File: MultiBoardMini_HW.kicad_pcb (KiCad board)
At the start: 2 copper layers, 63 x 63 mm, 52 parts, among them J1 PB0, J2 PA10, J3 Conn_01x02_Male, J4 PA10, J6 Conn_01x04, SW1 PF1, SW2 RESET, SW3 SW_Push_DPDT, SW5 SW_Push_DPDT, T3 PTS_1.5_2, U1 M78AR5-1, U2 NUCLEO-F303K8, U3 ESP32-C3-WROOM-02-N4, U4 TB67H303HG, U5 TB67H303HG, U6 MCP2562-E_SN

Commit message: 配線一応できた
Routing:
- net +5V: track 3.38 -> 145.1 mm
- net Net-(ENC/IO_2-Pin_4): track 0.00 -> 79.1 mm, vias 0 -> 5
- net Net-(ENC/IO_2-Pin_3): track 0.00 -> 66.0 mm, vias 0 -> 2
- net Net-(U2A-PA8): track 0.00 -> 64.9 mm, vias 0 -> 3
- net +3V3: track 84.7 -> 142.9 mm, vias 0 -> 2
- net Net-(D1-A): track 0.00 -> 56.5 mm, vias 0 -> 6
- net Net-(J6-Pin_1): track 0.00 -> 50.8 mm, vias 0 -> 3
- net Net-(U2B-PA5): track 0.00 -> 43.3 mm
- net Net-(U2A-NRST_1): track 0.00 -> 43.0 mm, vias 0 -> 1
- net Net-(U2B-PB3): track 0.00 -> 40.9 mm, vias 0 -> 1
- net Net-(U2A-PB0): track 0.00 -> 39.5 mm, vias 0 -> 2
- net Net-(U2A-PB4): track 0.00 -> 37.8 mm, vias 0 -> 1
- net Net-(J6-Pin_2): track 0.00 -> 36.0 mm, vias 0 -> 1
- net Net-(U2A-PB1): track 0.00 -> 35.9 mm, vias 0 -> 1
- net Net-(U4-VREG): track 0.00 -> 34.1 mm, vias 0 -> 1
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
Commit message: 配線一応完了 DRC確認済み
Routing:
- net GND: vias 114 -> 122
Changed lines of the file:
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@@
   (via (at 9 -8.5) (size 0.8) (drill 0.4) (layers "F.Cu" "B.Cu") (free) (net 2))
   (via (at -11.95 4.95) (size 0.5) (drill 0.3) (layers "F.Cu" "B.Cu") (free) (net 2))
+  (via (at -15 30) (size 0.8) (drill 0.4) (layers "F.Cu" "B.Cu") (free) (net 2))
+  (via (at 12.5 30) (size 0.8) (drill 0.4) (layers "F.Cu" "B.Cu") (free) (net 2))
+  (via (at 10.5 30) (size 0.8) (drill 0.4) (layers "F.Cu" "B.Cu") (free) (net 2))
+  (via (at -13 30) (size 0.8) (drill 0.4) (layers "F.Cu" "B.Cu") (free) (net 2))
   (via (at -13.75 -11.75) (size 0.5) (drill 0.3) (layers "F.Cu" "B.Cu") (free) (net 2))
   (via (at 16.75 12.25) (size 0.8) (drill 0.4) (layers "F.Cu" "B.Cu") (free) (net 2))
@@
   (via (at -12.4 9.8) (size 0.5) (drill 0.3) (layers "F.Cu" "B.Cu") (free) (net 2))
   (via (at 10 4) (size 0.8) (drill 0.4) (layers "F.Cu" "B.Cu") (free) (net 2))
+  (via (at -11 30) (size 0.8) (drill 0.4) (layers "F.Cu" "B.Cu") (free) (net 2))
   (via (at 14 -17.6) (size 0.5) (drill 0.3) (layers "F.Cu" "B.Cu") (net 2))
   (via (at 8.25 18.25) (size 0.8) (drill 0.4) (layers "F.Cu" "B.Cu") (free) (net 2))
@@
   (via (at 6.25 -13) (size 0.5) (drill 0.3) (layers "F.Cu" "B.Cu") (free) (net 2))
   (via (at -13.75 -12.5) (size 0.5) (drill 0.3) (layers "F.Cu" "B.Cu") (free) (net 2))
+  (via (at -17 30) (size 0.8) (drill 0.4) (layers "F.Cu" "B.Cu") (free) (net 2))
   (via (at 18 -1) (size 0.8) (drill 0.4) (layers "F.Cu" "B.Cu") (free) (net 2))
   (via (at 18.25 9.25) (size 0.8) (drill 0.4) (layers "F.Cu" "B.Cu") (free) (net 2))
@@
   (via (at 10.45 -12.7) (size 0.5) (drill 0.3) (layers "F.Cu" "B.Cu") (free) (net 2))
   (via (at 16.5 -2.25) (size 0.8) (drill 0.4) (layers "F.Cu" "B.Cu") (free) (net 2))
+  (via (at 14.5 30) (size 0.8) (drill 0.4) (layers "F.Cu" "B.Cu") (free) (net 2))
   (via (at -28.5 -12.5) (size 0.8) (drill 0.4) (layers "F.Cu" "B.Cu") (free) (net 2))
   (via (at 8.25 19.75) (size 0.8) (drill 0.4) (layers "F.Cu" "B.Cu") (free) (net 2))
   (via (at 10 1) (size 0.8) (drill 0.4) (layers "F.Cu" "B.Cu") (free) (net 2))
   (via (at -13.75 -13.25) (size 0.5) (drill 0.3) (layers "F.Cu" "B.Cu") (free) (net 2))
+  (via (at 16.5 30) (size 0.8) (drill 0.4) (layers "F.Cu" "B.Cu") (free) (net 2))
   (via (at -30 -12.5) (size 0.8) (drill 0.4) (layers "F.Cu" "B.Cu") (free) (net 2))
   (segment (start 5.45 -18) (end 7.44 -18) (width 0.4) (layer "B.Cu") (net 2))
@@
   (segment (start -19.2989 -1.7989) (end -21 -3.5) (width 0.25) (layer "F.Cu") (net 25))
   (segment (start -18.4024 8.5764) (end -19.2989 7.6799) (width 0.25) (layer "F.Cu") (net 25))
-  (segment (start 0.0257 -10.475) (end -2.88 -10.475) (width 0.25) (layer "F.Cu") (net 40))
-  (segment (start 5.4556 -14.3737) (end 3.9244 -14.3737) (width 0.25) (layer "F.Cu") (net 40))
+  (segment (start 5.5819 -14.5) (end 3.982616 -14.5) (width 0.25) (layer "F.Cu") (net 40))
+  (segment (start 6.655 -15.5731) (end 5.5819 -14.5) (width 0.25) (layer "F.Cu") (net 40))
+  (segment (start -0.042384 -10.475) (end -2.88 -10.475) (width 0.25) (layer "F.Cu") (net 40))
+  (segment (start 3.982616 -14.5) (end -0.042384 -10.475) (width 0.25) (layer "F.Cu") (net 40))
   (segment (start 6.655 -16.65) (end 6.655 -15.5731) (width 0.25) (layer "F.Cu") (net 40))
-  (segment (start 3.9244 -14.3737) (end 0.0257 -10.475) (width 0.25) (layer "F.Cu") (net 40))
-  (segment (start 6.655 -15.5731) (end 5.4556 -14.3737) (width 0.25) (layer "F.Cu") (net 40))
   (segment (start 2.4467 -16.2517) (end 2.845 -16.65) (width 0.25) (layer "F.Cu") (net 41))
   (segment (start 2.0693 -16.2517) (end 2.4467 -16.2517) (width 0.25) (layer "F.Cu") (net 41))

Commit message: ほぼ完成みたいなもの
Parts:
- added REF4: MountingHole_3.2mm_M3, MountingHole:MountingHole_3.2mm_M3, F.Cu at (-27.5, 27.5)
- added REF4: MountingHole_3.2mm_M3, MountingHole:MountingHole_3.2mm_M3, F.Cu at (27.5, -27.5)
- added REF4: MountingHole_3.2mm_M3, MountingHole:MountingHole_3.2mm_M3, F.Cu at (27.5, 27.5)
- added REF4: MountingHole_3.2mm_M3, MountingHole:MountingHole_3.2mm_M3, F.Cu at (-27.5, -27.5)
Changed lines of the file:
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@@
     )
+  )
+  (footprint "MountingHole:MountingHole_3.2mm_M3" (layer "F.Cu")
+    (at -27.5 27.5)
+    (descr "Mounting Hole 3.2mm, no annular, M3")
+    (tags "mounting hole 3.2mm no annular m3")
+    (attr exclude_from_pos_files exclude_from_bom)
+    (fp_text reference "REF4" (at 0 -4.2) (layer "F.SilkS") hide
+        (effects (font (size 1 1) (thickness 0.15)))
+    )
+    (fp_text value "MountingHole_3.2mm_M3" (at 0 4.2) (layer "F.Fab") hide
+        (effects (font (size 1 1) (thickness 0.15)))
+    )
+    (fp_text user "${REFERENCE}" (at 0.3 0) (layer "F.Fab") hide
+        (effects (font (size 1 1) (thickness 0.15)))
+    )
+    (fp_circle (center 0 0) (end 3.2 0)
+      (stroke (width 0.15) (type solid)) (fill none) (layer "Cmts.User"))
+    (fp_circle (center 0 0) (end 3.45 0)
+      (stroke (width 0.05) (type solid)) (fill none) (layer "F.CrtYd"))
+    (pad "" np_thru_hole circle (at 0 0) (size 3.2 3.2) (drill 3.2) (layers "F&B.Cu" "*.Mask"))
   )
   (footprint "Connector_PinHeader_2.54mm:PinHeader_1x03_P2.54mm_Vertical" (layer "F.Cu")
@@
       (rotate (xyz 0 0 0))
     )
+  )
+  (footprint "MountingHole:MountingHole_3.2mm_M3" (layer "F.Cu")
+    (at 27.5 -27.5)
+    (descr "Mounting Hole 3.2mm, no annular, M3")
+    (tags "mounting hole 3.2mm no annular m3")
+    (attr exclude_from_pos_files exclude_from_bom)
+    (fp_text reference "REF4" (at 0 -4.2) (layer "F.SilkS") hide
+        (effects (font (size 1 1) (thickness 0.15)))
+    )
+    (fp_text value "MountingHole_3.2mm_M3" (at 0 4.2) (layer "F.Fab") hide
+        (effects (font (size 1 1) (thickness 0.15)))
+    )
+    (fp_text user "${REFERENCE}" (at 0.3 0) (layer "F.Fab") hide
+        (effects (font (size 1 1) (thickness 0.15)))
+    )
+    (fp_circle (center 0 0) (end 3.2 0)
+      (stroke (width 0.15) (type solid)) (fill none) (layer "Cmts.User"))
+    (fp_circle (center 0 0) (end 3.45 0)
+      (stroke (width 0.05) (type solid)) (fill none) (layer "F.CrtYd"))
+    (pad "" np_thru_hole circle (at 0 0) (size 3.2 3.2) (drill 3.2) (layers "F&B.Cu" "*.Mask"))
+  )
+  (footprint "MountingHole:MountingHole_3.2mm_M3" (layer "F.Cu")
+    (at 27.5 27.5)
+    (descr "Mounting Hole 3.2mm, no annular, M3")
+    (tags "mounting hole 3.2mm no annular m3")
+    (attr exclude_from_pos_files exclude_from_bom)
+    (fp_text reference "REF4" (at 0 -4.2) (layer "F.SilkS") hide
+        (effects (font (size 1 1) (thickness 0.15)))
+    )
+    (fp_text value "MountingHole_3.2mm_M3" (at 0 4.2) (layer "F.Fab") hide
+        (effects (font (size 1 1) (thickness 0.15)))
+    )
+    (fp_text user "${REFERENCE}" (at 0.3 0) (layer "F.Fab") hide
+        (effects (font (size 1 1) (thickness 0.15)))
+    )
+    (fp_circle (center 0 0) (end 3.2 0)
+      (stroke (width 0.15) (type solid)) (fill none) (layer "Cmts.User"))
+    (fp_circle (center 0 0) (end 3.45 0)
+      (stroke (width 0.05) (type solid)) (fill none) (layer "F.CrtYd"))
+    (pad "" np_thru_hole circle (at 0 0) (size 3.2 3.2) (drill 3.2) (layers "F&B.Cu" "*.Mask"))
   )
   (footprint "MultiBoardMini_Libraries:PTS_1.5_2" (layer "F.Cu")
@@
       (net 2 "GND") (pinfunction "C") (pintype "passive") (solder_mask_margin 0.102))
   )
+  (footprint "MountingHole:MountingHole_3.2mm_M3" (layer "F.Cu")
+    (at -27.5 -27.5)
+    (descr "Mounting Hole 3.2mm, no annular, M3")
+    (tags "mounting hole 3.2mm no annular m3")
+    (attr exclude_from_pos_files exclude_from_bom)
+    (fp_text reference "REF4" (at 0 -4.2) (layer "F.SilkS") hide
+        (effects (font (size 1 1) (thickness 0.15)))
+    )
+    (fp_text value "MountingHole_3.2mm_M3" (at 0 4.2) (layer "F.Fab") hide
+        (effects (font (size 1 1) (thickness 0.15)))
+    )
+    (fp_text user "${REFERENCE}" (at 0.3 0) (layer "F.Fab") hide
+        (effects (font (size 1 1) (thickness 0.15)))
+    )
+    (fp_circle (center 0 0) (end 3.2 0)
+      (stroke (width 0.15) (type solid)) (fill none) (layer "Cmts.User"))
+    (fp_circle (center 0 0) (end 3.45 0)
+      (stroke (width 0.05) (type solid)) (fill none) (layer "F.CrtYd"))
+    (pad "" np_thru_hole circle (at 0 0) (size 3.2 3.2) (drill 3.2) (layers "F&B.Cu" "*.Mask"))
+  )
   (footprint "Button_Switch_SMD:SW_Push_1P1T_NO_Vertical_Wuerth_434133025816" (layer "F.Cu")

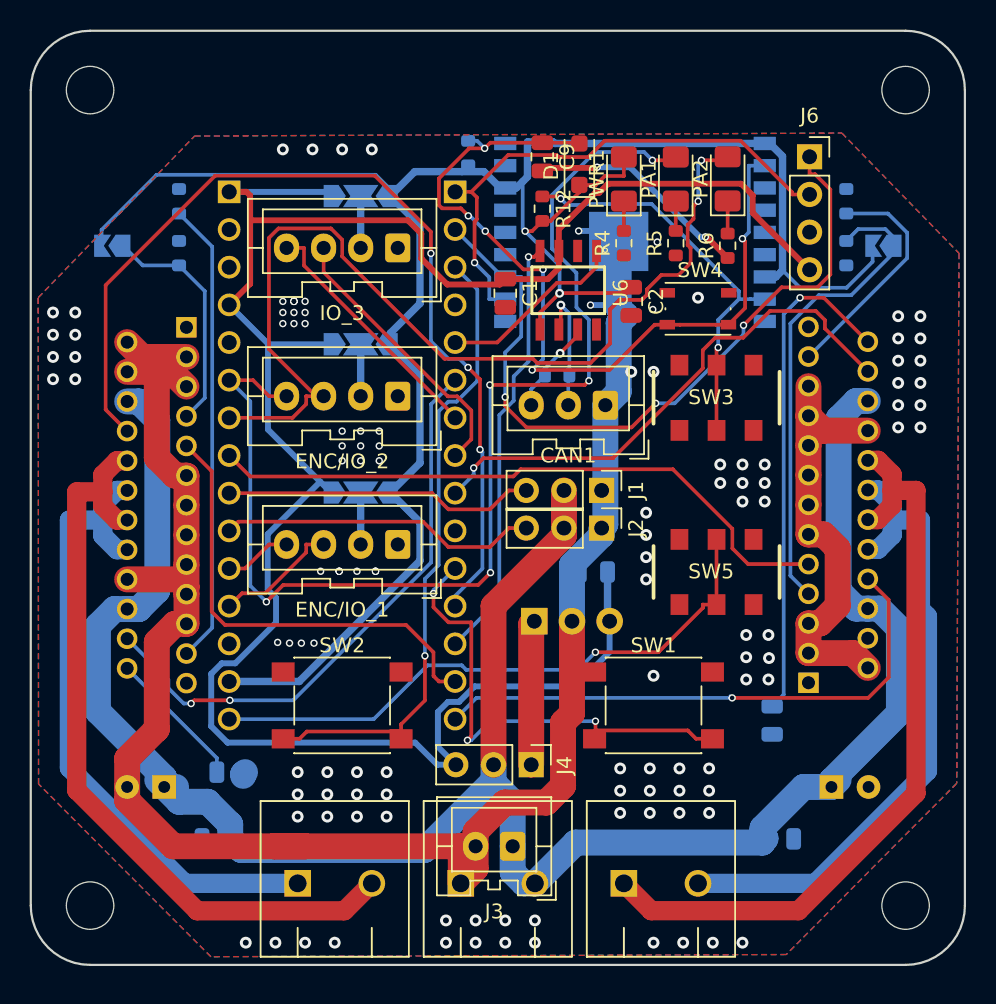
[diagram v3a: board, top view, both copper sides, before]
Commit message: 緊急発注用
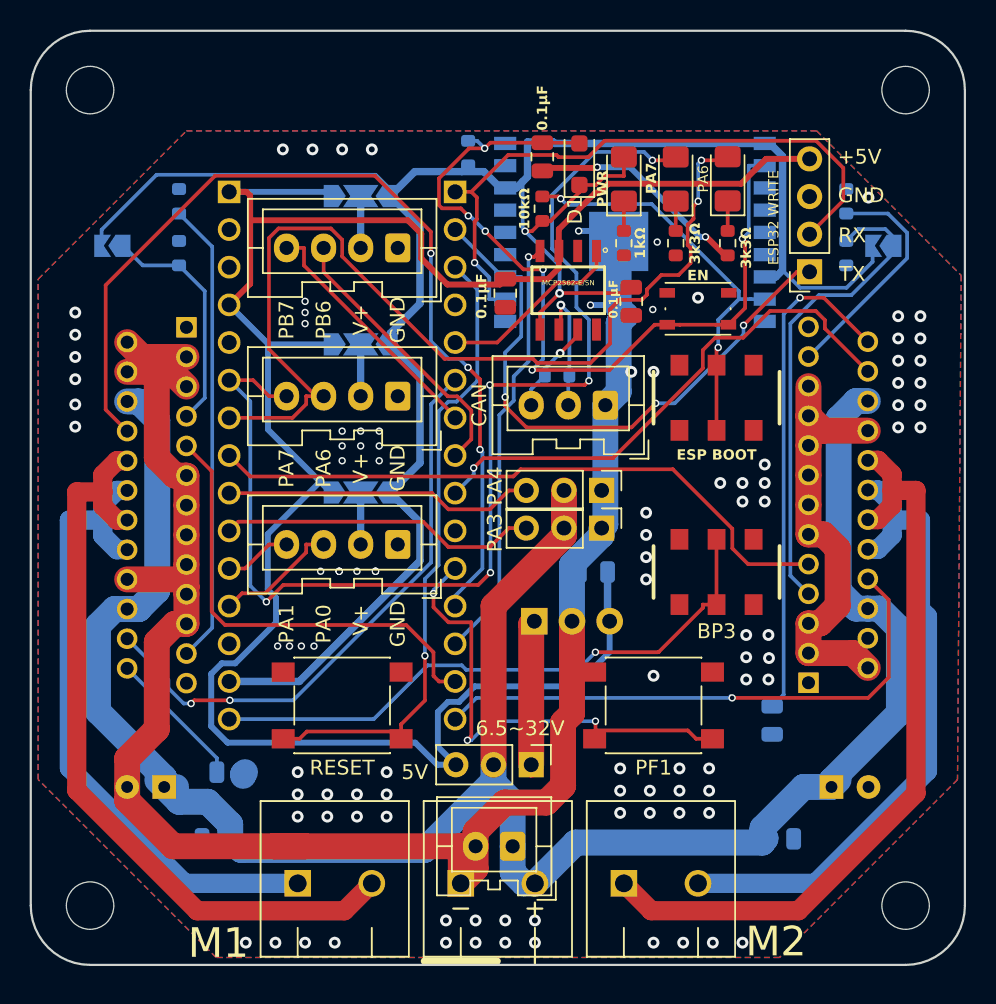
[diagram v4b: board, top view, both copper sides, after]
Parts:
- 10kΩ: renamed from R12; value 10k -> 10kΩ
- 3V3 5V: renamed from JP3
- ESP BOOT: renamed from SW3
- M1 ON: renamed from MJP2
- M2 ON: renamed from MJP1
- Nucleo F303K8: renamed from U2
- moved GND 7.76 mm to (21.0, -15.2), turned to 180 degrees
- moved 3k3Ω 0.18 mm to (15.5, -17.2)
- renumbered C9 to 0.1μF, C1 to 0.1μF, C2 to 0.1μF, R2 to 10kΩ, R3 to 10kΩ, R1 to 120Ω, R4 to 1kΩ, R6 to 3k3Ω, R5 to 3k3Ω, C12 to 47μF, C5 to 47μF, R7 to 51kΩ, R13 to 51kΩ, J4 to 6.5~32V, SW5 to BP3, CAN1 to CAN, SW4 to EN, U3 to ESP32-C3-WROOM-02-N4, J6 to GND, U6 to MCP2562-E/SN, J2 to PA3, J1 to PA4, PA2 to PA6, PA1 to PA7, SW1 to PF1, PWR1 to PWR, SW2 to RESET
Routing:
- net Net-(J6-Pin_1): track 50.8 -> 40.8 mm
- net Net-(J6-Pin_2): track 36.0 -> 42.8 mm
- net +5V: track 145.1 -> 142.6 mm
- net GND: vias 122 -> 107
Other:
- board text added: "+5V"
- board text added: "0.1μF"
- board text added: "3V3 5V"
- board text added: "4.7μF"
- board text added: "5V"
- board text added: "ESP32 WRITE"
- board text added: "GND"
- board text added: "M1"
- board text added: "M2"
- board text added: "MultiBoardMini Ver0.4 UGOKU Lab 2023-10"
- board text added: "PA0"
- board text added: "PA1"
- board text added: "PA6"
- board text added: "PA7"
- board text added: "PB6"
- board text added: "PB7"
- board text added: "RX"
- board text added: "TX"
- board text added: "V+"
- board text added: "https://github.com/UGOKU-Lab/MultiBoardMini_HW"

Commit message: 改良版の電源配線暫定版
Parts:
- added JP4: Jumper_NC_Dual, Jumper:SolderJumper-3_P2.0mm_Open_TrianglePad1.0x1.5mm, B.Cu at (4.50, 5.25)
- C10, R9: moved to F.Cu
- JP3: renamed from 3V3 5V
- MJP1: renamed from M2 ON
- MJP2: renamed from M1 ON
- PA6, PA7: footprint LED_SMD:LED_1206_3216Metric_Pad1.42x1.75mm_HandSolder -> LED_SMD:LED_0805_2012Metric_Pad1.15x1.40mm_HandSolder
- PWR1: renamed from PWR; footprint LED_SMD:LED_1206_3216Metric_Pad1.42x1.75mm_HandSolder -> LED_SMD:LED_0805_2012Metric_Pad1.15x1.40mm_HandSolder
- R12: renamed from 10kΩ; value 10kΩ -> 10k
- SW1: renamed from PF1; footprint Button_Switch_SMD:SW_Push_1P1T_NO_6x6mm_H9.5mm -> Button_Switch_THT:SW_PUSH_6mm
- SW2: renamed from RESET; footprint Button_Switch_SMD:SW_Push_1P1T_NO_6x6mm_H9.5mm -> Button_Switch_THT:SW_PUSH_6mm
- SW3: renamed from ESP BOOT; footprint MultiBoardMini_Libraries:SSSS213202 -> MultiBoardMini_Libraries:IS-2235
- SW4: renamed from EN; footprint Button_Switch_SMD:SW_Push_1P1T_NO_Vertical_Wuerth_434133025816 -> Button_Switch_THT:SW_PUSH_1P1T_6x3.5mm_H4.3_APEM_MJTP1243
- SW5: renamed from BP3; footprint MultiBoardMini_Libraries:SSSS213202 -> MultiBoardMini_Libraries:IS-2235
- U2: renamed from Nucleo F303K8
- moved C13 32.0 mm to (26.5, -16.0), turned to 180 degrees
- moved R9 18.0 mm to (13.6, -14.2), turned to 90 degrees
- moved R12 14.0 mm to (16.0, -14.2), turned to 90 degrees
- moved C9 12.8 mm to (15.8, -21.4)
- moved C1 10.5 mm to (11.0, -14.2)
- moved C2 8.52 mm to (0.50, -13.8)
- moved D1 7.54 mm to (13.0, -21.8), turned to -90 degrees
- moved R6 5.47 mm to (10.2, -18.7)
- moved PA6 5.35 mm to (10.2, -22.5)
- moved SW4 5.27 mm to (11.8, -7.75)
- moved R5 5.23 mm to (7.00, -18.7)
- moved PA7 5.10 mm to (7.00, -22.5)
- moved R4 4.99 mm to (3.75, -18.7)
- moved PWR1 4.86 mm to (3.75, -22.5)
- moved SW3 4.81 mm to (15.0, -1.95)
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- renumbered 0.1μF to C1, 47μF to C12, 0.1μF to C2, 47μF to C5, 0.1μF to C9, CAN to CAN1, PA4 to J1, PA3 to J2, 6.5~32V to J4, GND to J6, 120Ω to R1, 51kΩ to R13, 10kΩ to R2, 10kΩ to R3, 1kΩ to R4, 3k3Ω to R5, 3k3Ω to R6, 51kΩ to R7, ESP32-C3-WROOM-02-N4 to U3, MCP2562-E/SN to U6
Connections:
- J1 pad 2: PWR -> Net-(J1-Pin_2)
- J2 pad 2: PWR -> Net-(J1-Pin_2)
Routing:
- net +3V3: track 142.9 -> 0.00 mm, vias 2 -> 0
- net +5V: track 142.6 -> 7.09 mm
- net Net-(ENC/IO_2-Pin_4): track 79.1 -> 0.00 mm, vias 5 -> 0
- net Net-(ENC/IO_2-Pin_3): track 66.0 -> 0.00 mm, vias 2 -> 0
- net Net-(U2A-PA8): track 64.9 -> 0.00 mm, vias 3 -> 0
- net Net-(D1-A): track 56.5 -> 0.00 mm, vias 6 -> 0
- net Net-(U2B-PA5): track 43.3 -> 0.00 mm
- net Net-(U2A-NRST_1): track 43.0 -> 0.00 mm, vias 1 -> 0
- net Net-(J6-Pin_2): track 42.8 -> 0.00 mm, vias 1 -> 0
- net Net-(U2B-PB3): track 40.9 -> 0.00 mm, vias 1 -> 0
- net Net-(J6-Pin_1): track 40.8 -> 0.00 mm, vias 3 -> 0
- net Net-(U2A-PB0): track 39.5 -> 0.00 mm, vias 2 -> 0
- net Net-(U2A-PB4): track 37.8 -> 0.00 mm, vias 1 -> 0
- net Net-(U2A-PB1): track 35.9 -> 0.00 mm, vias 1 -> 0
- net Net-(U4-VREG): track 34.1 -> 0.00 mm, vias 1 -> 0
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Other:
- board text added: "DL"
- board text added: "MultiBoardMini Ver0.41 UGOKU Lab 2023-10"
- board text removed: "MultiBoardMini Ver0.4 UGOKU Lab 2023-10"
